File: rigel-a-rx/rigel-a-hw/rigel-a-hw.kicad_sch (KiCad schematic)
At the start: 18 parts, among them U1 STM32WLE5C8Ux, U2 XC6206P332MR, U3 CH340E, U4 TYPE-C_16PIN_2MD(073)

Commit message: schematic mostly done except pi filter
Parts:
- removed U3: CH340E, jlc:MSOP-10_L3.0-W3.0-P0.50-LS5.0-BL, symbol default_lib:CH340E
- added C13, C14, C15, C16: C_Small, symbol Device:C_Small
- added C17: 10nF, symbol Device:C_Small
- added C18: 10pF, symbol Device:C_Small
- added IC1: BALFHB-WL-02D3, BALFHBWL02D3, symbol BALFHB-WL-02D3:BALFHB-WL-02D3
- added J1: Conn_01x03_Pin, symbol Connector:Conn_01x03_Pin
- added J2: Conn_Coaxial, symbol Connector:Conn_Coaxial
- added L1: L_Small, symbol Device:L_Small
- added LED1: FM-B2020RGBA-HG, jlc:LED-SMD_FM-B2020RGBA-HG, symbol default_lib:FM-B2020RGBA-HG
- added R3: 4.7k, symbol Device:R
- added R4: 220, symbol Device:R
- added R5: 120, symbol Device:R
- added R6: 33, symbol Device:R
- added R7: 47, symbol Device:R
- added U3: CH340X, jlc:MSOP-10_L3.0-W3.0-P0.50-LS5.0-BL, symbol default_lib:CH340X
- added U5: X1G004131004200, jlc:OSC-SMD_4P-L2.0-W1.6-BL_EPSON_TG-5006CJ-19H, symbol default_lib:X1G004131004200
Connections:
- net +3.3V: now also LED1.3 (A), U3.10 (V3), U3.7 (VCC)
- net GND: now also C13.2, C15.1, C16.1, C17.1, IC1.B1 (GND2), IC1.B2 (GND3), IC1.C2 (GND1), J1.1 (Pin_1), J2.2 (Ext), R3.1, U3.3 (GND), U5.2 (GND)
- net USBD+: now also U3.1 (UD+)
- net USBD-: now also U3.2 (UD-)
- net at U1.10 (PA3): now also U3.8 (TXD)
- net TIM1_CH1_RED: now reaches U1.16 (PA8)
- net TIM1_CH1_RED: now also R5.2
- net TIM1_CH2_GREEN: now reaches U1.17 (PA9)
- net TIM1_CH2_GREEN: now also R7.2
- net RESET: now reaches U1.18 (NRST)
- net RESET: now also U3.4 (RTS#)
- net BOOT0: now reaches U1.19 (PH3)
- net BOOT0: now also R3.2, U3.6 (TNOW/DTR#)
- net RFI+: now reaches U1.20 (RFI_P)
- net RFI+: now also IC1.A3 (RFI_P_OUT)
- net RFI-: now reaches U1.21 (RFI_N)
- net RFI-: now also IC1.A2 (RFI_N_OUT)
- net OSC_IN: now reaches U1.26 (OSC_IN)
- net OSC_IN: now also C18.2
- net PB0-VDD_TCXO: now reaches U1.30 (PB0)
- net PB0-VDD_TCXO: now also C17.2, U5.4 (VCC)
- net TIM3_CH3_BLUE: now reaches U1.33 (PA10)
- net TIM3_CH3_BLUE: now also R6.2
- net JTMS/SWDIO: now reaches U1.36 (PA13)
- net JTMS/SWDIO: now also J1.3 (Pin_3)
- net JTCK/SWCLK: now reaches U1.42 (PA14)
- net JTCK/SWCLK: now also J1.2 (Pin_2)
- net at U1.9 (PA2): now also U3.9 (RXD)
- new net: C14.1, C15.2, L1.2
- new net: C13.1, C14.2, IC1.C3 (RFI_IN)
- new net: R4.1, U5.3 (OUT)
- new net: C18.1, R4.2
- new net: C16.2, J2.1 (In), L1.1
- new net: LED1.1 (K), R5.1
- new net: LED1.2 (K), R6.1
- new net: LED1.4 (K), R7.1
- no-connect marks 9 -> 13
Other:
- note added: "Higher duty = lower brightness"
- note added: "PA2 - USART2_TX PA3 - USART2_RX"
- note added: "Should be 3V"
- moved on the sheet: C10, C12, U2

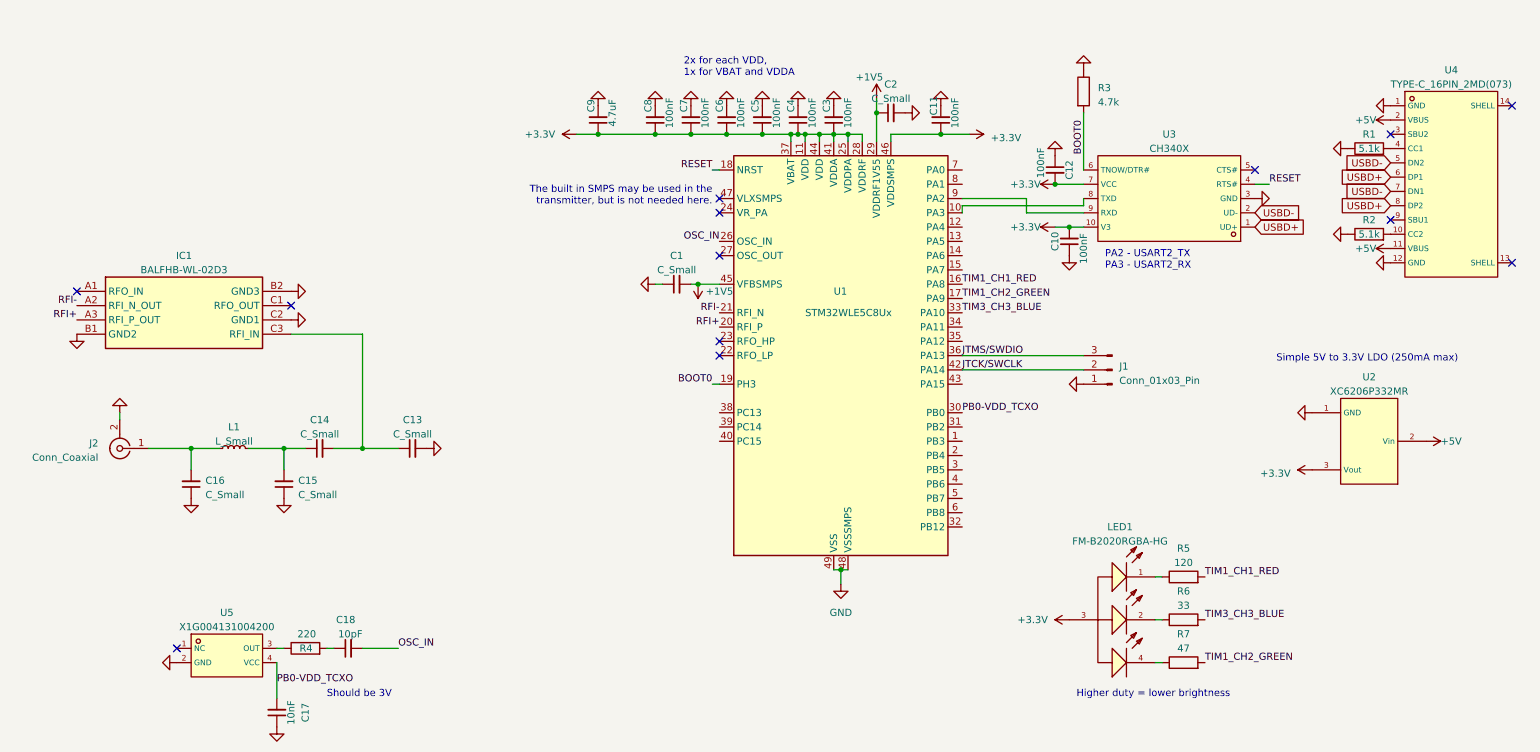
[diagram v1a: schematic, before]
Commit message: begin sw and finish schematic (pre kicad 8)
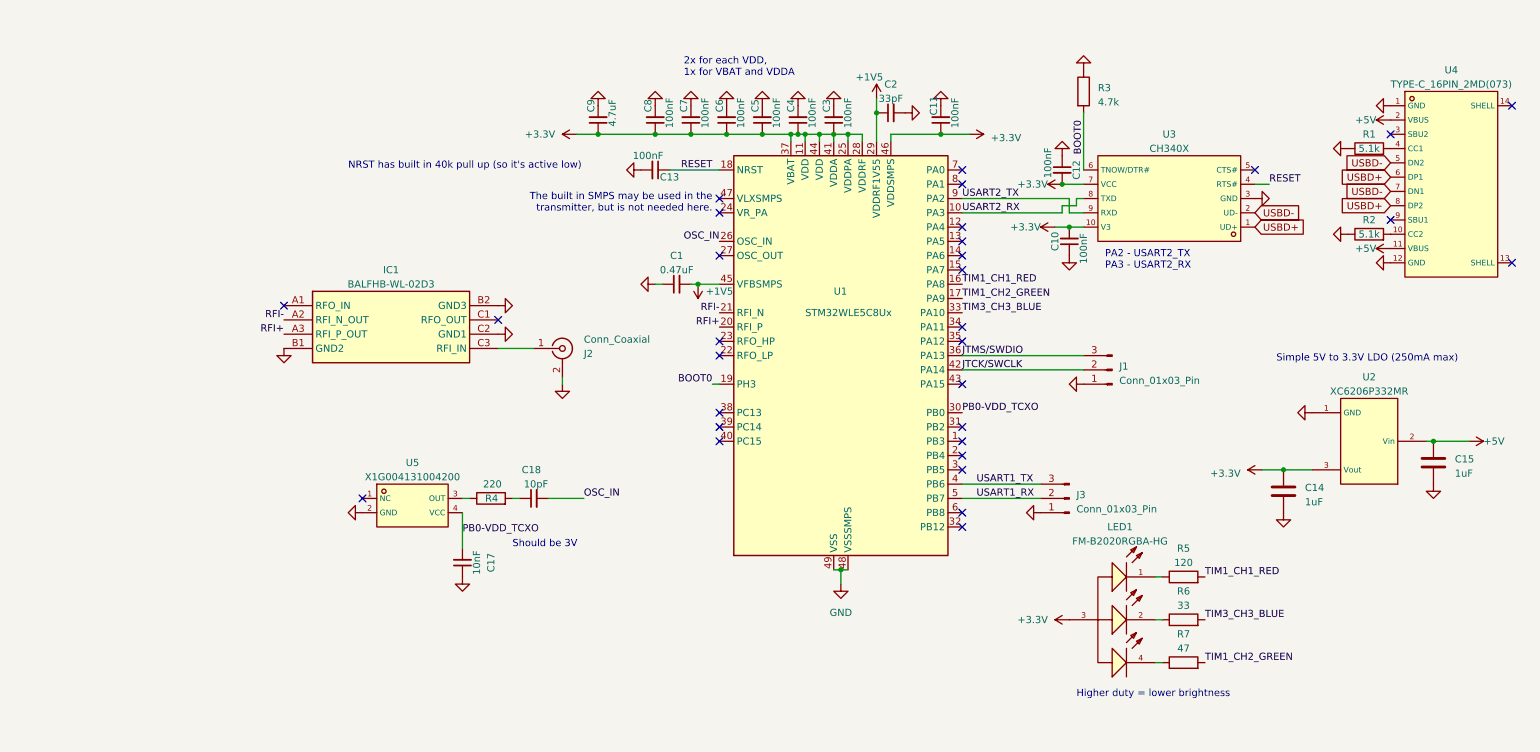
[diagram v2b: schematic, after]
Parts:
- removed C14, C15, C16: C_Small, symbol Device:C_Small
- removed L1: L_Small, symbol Device:L_Small
- added C14, C15: 1uF, Capacitor_SMD:C_0603_1608Metric, symbol Device:C
- added J3: Conn_01x03_Pin, Connector_PinSocket_2.54mm:PinSocket_1x03_P2.54mm_Vertical, symbol Connector:Conn_01x03_Pin
- C1: value C_Small -> 0.47uF; footprint (none) -> Capacitor_SMD:C_0603_1608Metric
- C10, C11, C12, C17, C18, C3, C4, C5, C6, C7, C8: footprint (none) -> Capacitor_SMD:C_0402_1005Metric
- C13: value C_Small -> 100nF; footprint (none) -> Capacitor_SMD:C_0402_1005Metric
- C2: value C_Small -> 33pF; footprint (none) -> Capacitor_SMD:C_0402_1005Metric
- C9: footprint (none) -> Capacitor_SMD:C_0603_1608Metric
- IC1: footprint BALFHBWL02D3 -> jlc:BALFHBWL02D3
- J1: footprint (none) -> Connector_PinSocket_2.54mm:PinSocket_1x03_P2.54mm_Vertical
- R1, R2, R3, R4: footprint (none) -> Resistor_SMD:R_0402_1005Metric
- R5, R6, R7: footprint (none) -> Resistor_SMD:R_0603_1608Metric
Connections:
- net +3.3V: now also C14.1
- net +5V: now also C15.1
- net GND: now also C14.2, C15.2, J3.1 (Pin_1)
- net RESET: now also C13.1
- net at IC1.C3 (RFI_IN): now also J2.1 (In); no longer C13.1
- net USART2_RX: now reaches U1.10 (PA3), U3.8 (TXD)
- net USART2_TX: now reaches U1.9 (PA2), U3.9 (RXD)
- net USART1_TX: now reaches U1.4 (PB6)
- net USART1_TX: now also J3.3 (Pin_3)
- net USART1_RX: now reaches U1.5 (PB7)
- net USART1_RX: now also J3.2 (Pin_2)
- no-connect marks 13 -> 31
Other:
- note added: "NRST has built in 40k pull up (so it's active low)"
- moved on the sheet: C12, C17, C18, IC1, J2, R4, U5

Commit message: migrate to v8
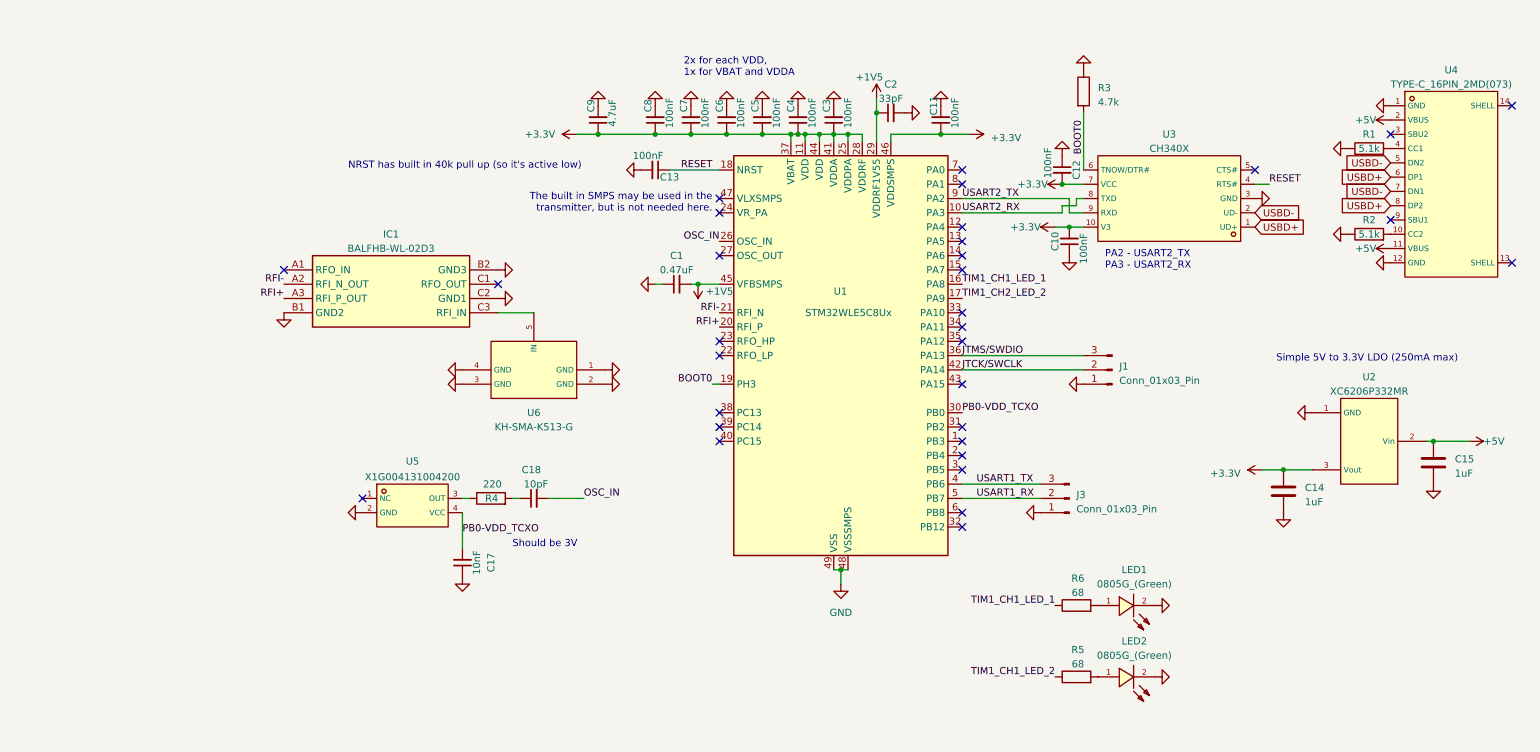
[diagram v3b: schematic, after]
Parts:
- removed J2: Conn_Coaxial, symbol Connector:Conn_Coaxial
- removed LED1: FM-B2020RGBA-HG, jlc:LED-SMD_FM-B2020RGBA-HG, symbol default_lib:FM-B2020RGBA-HG
- removed R7: 47, Resistor_SMD:R_0603_1608Metric, symbol Device:R
- added LED1, LED2: 0805G_(Green), jlc:LED0805-R-RD, symbol default_lib:0805G_(Green)
- added U6: KH-SMA-K513-G, jlc:ANT-TH_KH-SMA-K513-G, symbol default_lib:KH-SMA-K513-G
- R5: value 120 -> 68
- R6: value 33 -> 68
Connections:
- net GND: now also LED1.2 (K), LED2.2 (K), U6.1 (GND), U6.2 (GND), U6.3 (GND), U6.4 (GND)
- net TIM1_CH1_LED_2: now reaches R5.1
- net TIM1_CH1_LED_1: now reaches R6.1
- net TIM1_CH1_LED_1: now also U1.16 (PA8)
- net at IC1.C3 (RFI_IN): now also U6.5 (IN)
- net TIM1_CH1_RED: no longer names the net of R5.2
- net TIM1_CH1_RED: now also LED2.1 (A); no longer U1.16 (PA8)
- net TIM1_CH2_GREEN renamed TIM1_CH2_LED_2
- net TIM3_CH3_BLUE: no longer names the net of R6.2
- net TIM3_CH3_BLUE: now also LED1.1 (A); no longer U1.33 (PA10)
- no-connect marks 31 -> 32
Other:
- note removed: "Higher duty = lower brightness"
- moved on the sheet: IC1

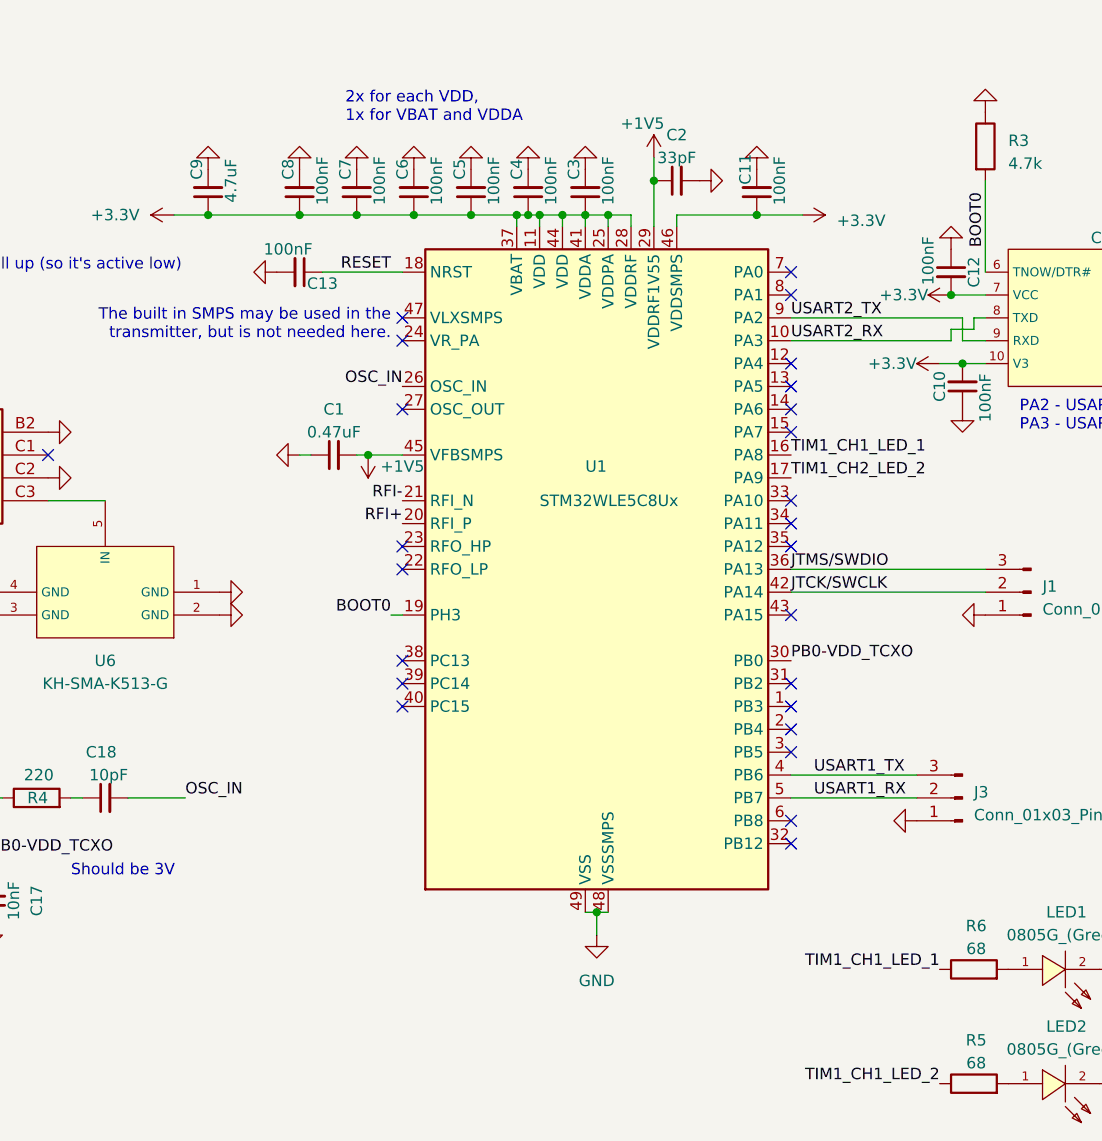
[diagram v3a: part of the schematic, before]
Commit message: Pretty much finish layout
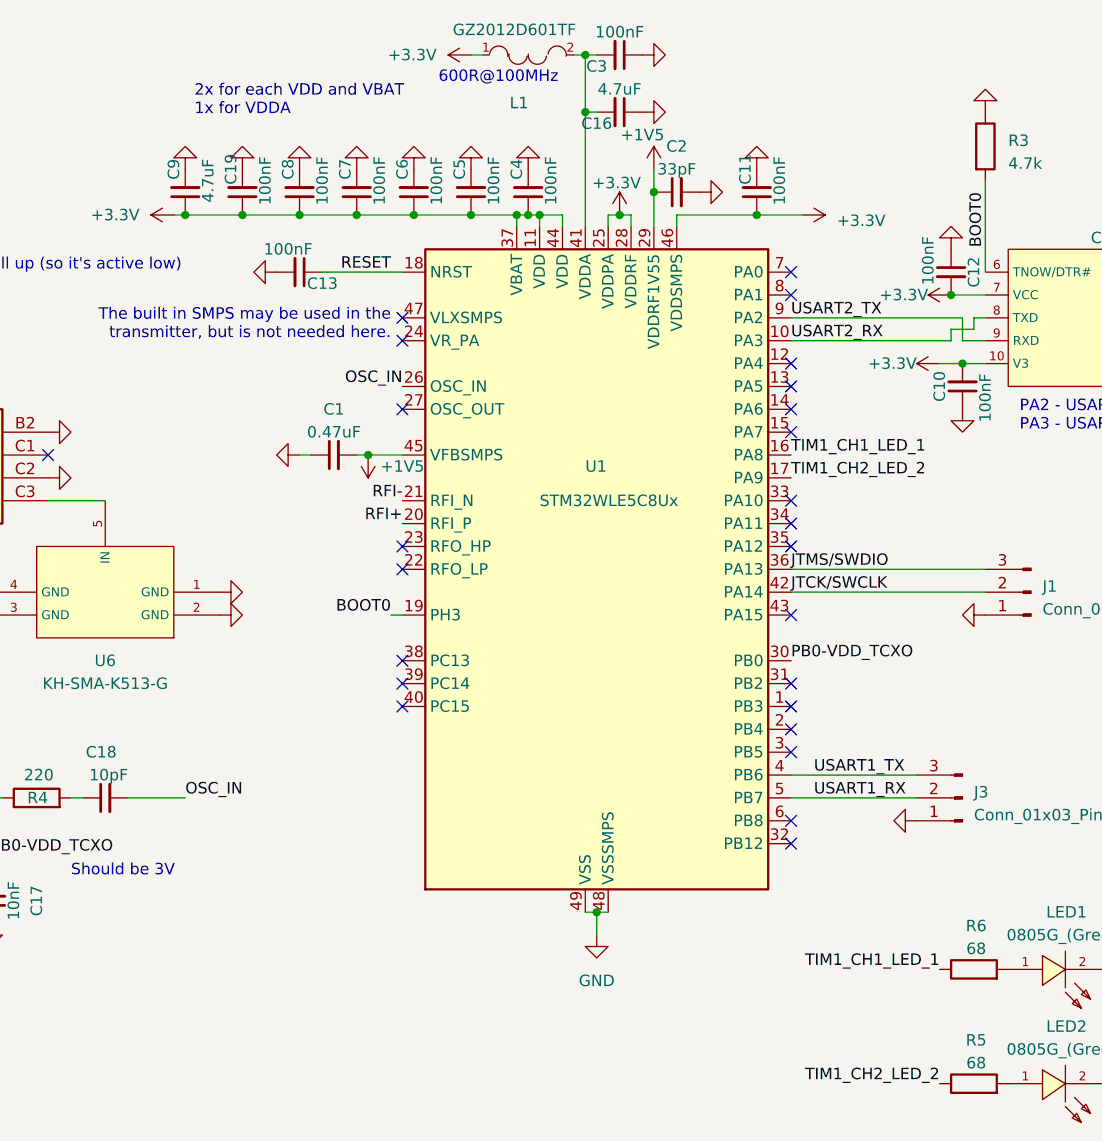
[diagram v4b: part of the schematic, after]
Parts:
- added C16: 4.7uF, Capacitor_SMD:C_0603_1608Metric, symbol Device:C_Small
- added C19: 100nF, Capacitor_SMD:C_0402_1005Metric, symbol Device:C_Small
- added L1: GZ2012D601TF, jlc:L0805, symbol default_lib:GZ2012D601TF
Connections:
- net TIM1_CH1_LED_2 is gone; now on net TIM1_CH2_LED_2: R5.1
- net +3.3V: now also C19.1, L1.1; no longer C3.1, U1.41 (VDDA)
- net GND: now also C3.1, C16.1, C19.2; no longer C3.2
- new net: C16.2, C3.2, L1.2, U1.41 (VDDA)
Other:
- note added: "2x for each VDD and VBAT 1x for VDDA"
- note added: "600R@100MHz"
- note removed: "2x for each VDD, 1x for VBAT and VDDA"
- moved on the sheet: C2, C3, C9

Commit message: add finishing touches to pcb
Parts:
- added H1, H2: MountingHole, MountingHole:MountingHole_2.2mm_M2, symbol Mechanical:MountingHole
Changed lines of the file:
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@@
+	)
+	(symbol
+		(lib_id "Mechanical:MountingHole")
+		(at 25.4 30.48 0)
+		(unit 1)
+		(exclude_from_sim no)
+		(in_bom yes)
+		(on_board yes)
+		(dnp no)
+		(fields_autoplaced yes)
+		(property "Reference" "H1"
+			(at 27.94 29.2099 0)
+			(effects
+				(font
+					(size 1.27 1.27)
+				)
+				(justify left)
+			)
+		)
+		(property "Value" "MountingHole"
+			(at 27.94 31.7499 0)
+			(effects
+				(font
+					(size 1.27 1.27)
+				)
+				(justify left)
+			)
+		)
+		(property "Footprint" "MountingHole:MountingHole_2.2mm_M2"
+			(at 25.4 30.48 0)
+			(effects
+				(font
+					(size 1.27 1.27)
+				)
+				(hide yes)
+			)
+		)
+		(property "Datasheet" "~"
+			(at 25.4 30.48 0)
+			(effects
+				(font
+					(size 1.27 1.27)
+				)
+				(hide yes)
+			)
+		)
+		(property "Description" "Mounting Hole without connection"
+			(at 25.4 30.48 0)
+			(effects
+				(font
+					(size 1.27 1.27)
+				)
+				(hide yes)
+			)
+		)
+		(instances
+			(project "rigel-a-hw"
+				(path "/5b772f1b-b884-4184-9180-5f1d0867ded9"
+					(reference "H1")
+					(unit 1)
+				)
+			)
+		)
 	)
 	(symbol
@@
 					(unit 1)
 				)
+			)
+		)
+	)
+	(symbol
+		(lib_id "Mechanical:MountingHole")
+		(at 25.4 35.56 0)
+		(unit 1)
+		(exclude_from_sim no)
+		(in_bom yes)
+		(on_board yes)
+		(dnp no)
+		(fields_autoplaced yes)
+		(property "Reference" "H2"
+			(at 27.94 34.2899 0)
+			(effects
+				(font
+					(size 1.27 1.27)
+				)
+				(justify left)
+			)
+		)
+		(property "Value" "MountingHole"
+			(at 27.94 36.8299 0)
+			(effects
+				(font
+					(size 1.27 1.27)
+				)
+				(justify left)
+			)
+		)
+		(property "Footprint" "MountingHole:MountingHole_2.2mm_M2"
+			(at 25.4 35.56 0)
+			(effects
+				(font
+					(size 1.27 1.27)
+				)
+				(hide yes)
+			)
+		)
+		(property "Datasheet" "~"
+			(at 25.4 35.56 0)
+			(effects
+				(font
+					(size 1.27 1.27)
+				)
+				(hide yes)
+			)
+		)
+		(property "Description" "Mounting Hole without connection"
+			(at 25.4 35.56 0)
+			(effects
+				(font
+					(size 1.27 1.27)
+				)
+				(hide yes)
+			)
+		)
+		(instances
+			(project "rigel-a-hw"
+				(path "/5b772f1b-b884-4184-9180-5f1d0867ded9"
+					(reference "H2")
+					(unit 1)
+				)
